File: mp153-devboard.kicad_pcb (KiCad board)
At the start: 4 copper layers, 39.9 x 57.9 mm, 117 parts, among them CON1 microSDCon_SMT_104031-0811, J1 Pins_02x04_RightAngle_P2.54mm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, J2 Pins_02x05_P1.27mm_SMT, J3 USB-C_Receptacle_Molex_217179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, J4 Pins_02x40_P0.4mm_W3.0mm_SMT, J5 Conn_01x02, J6 Pins_02x40_P0.4mm_W3.0mm_SMT, U13 NCP51460SN33, U14 DDR3L-RAM-4Gb_MT41K256M16TW, U15 AP6230xZ6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

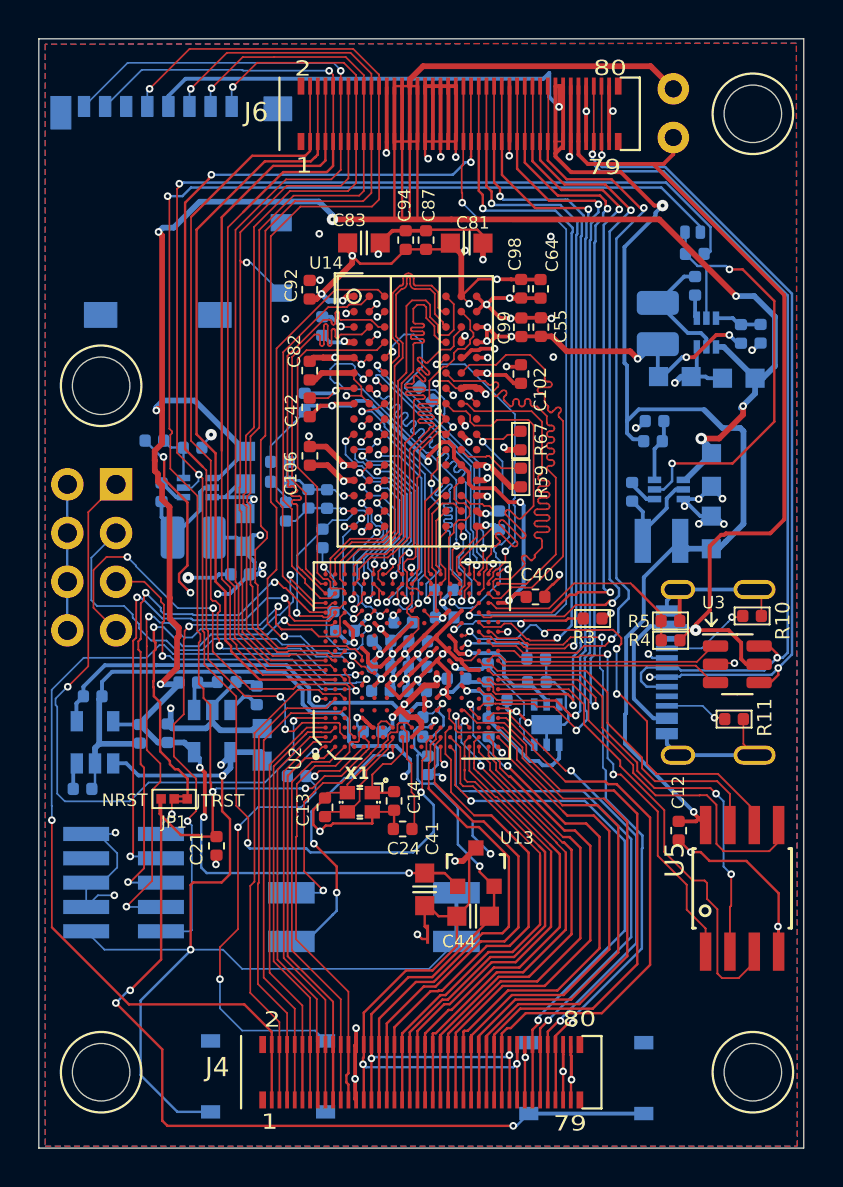
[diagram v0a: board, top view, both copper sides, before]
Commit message: devboard v0.1: increased spacing between zones on inner layers. Vias => 0.25mm holes
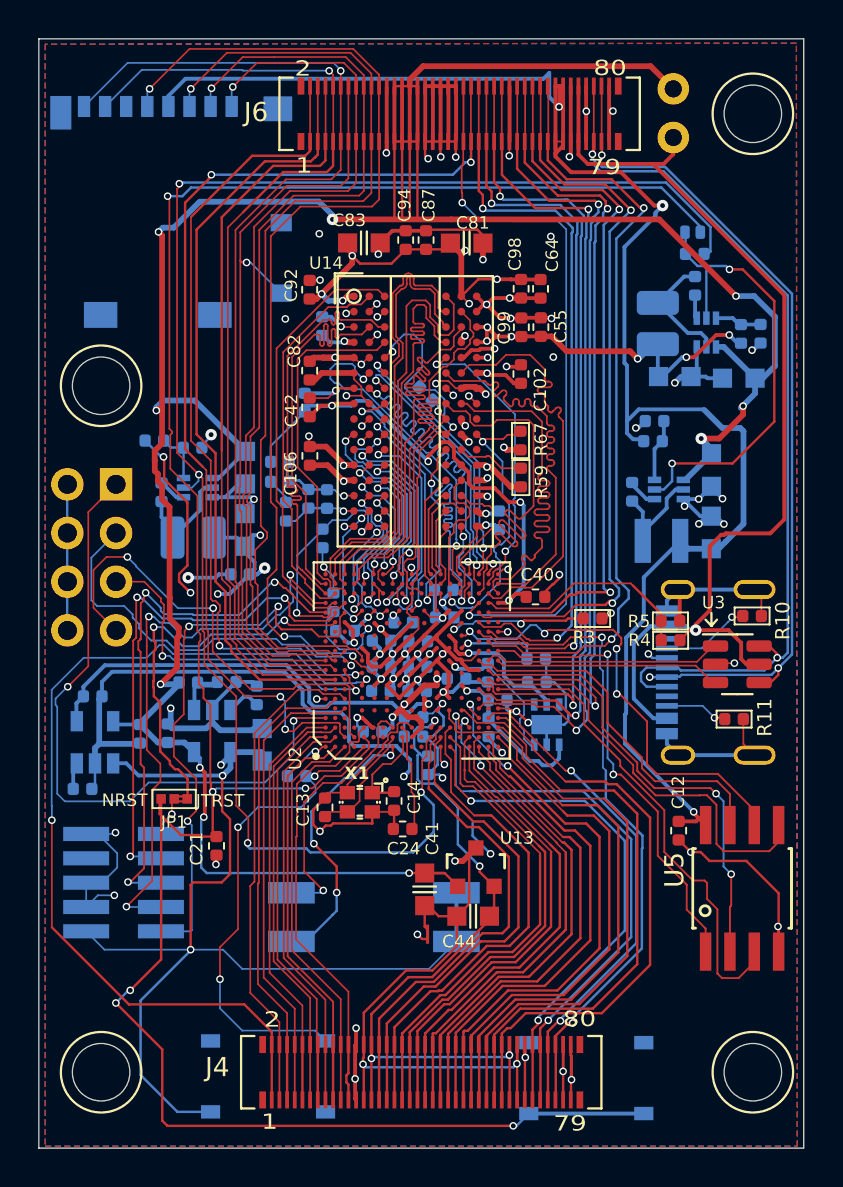
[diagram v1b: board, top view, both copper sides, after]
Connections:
- net /I2C2_SCL renamed /D25
- net /I2C2_SDA renamed /D14
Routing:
- net VDD_DDR: track 64.5 -> 78.0 mm
- net VDD_CORE: track 32.9 -> 32.6 mm, vias 11 -> 10
